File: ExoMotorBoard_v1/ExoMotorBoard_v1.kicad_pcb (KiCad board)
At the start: 2 copper layers, 3 parts, among them IC1 DSPIC33FJ128MC802-I_SP, U1 MIC5219-3.3YMM

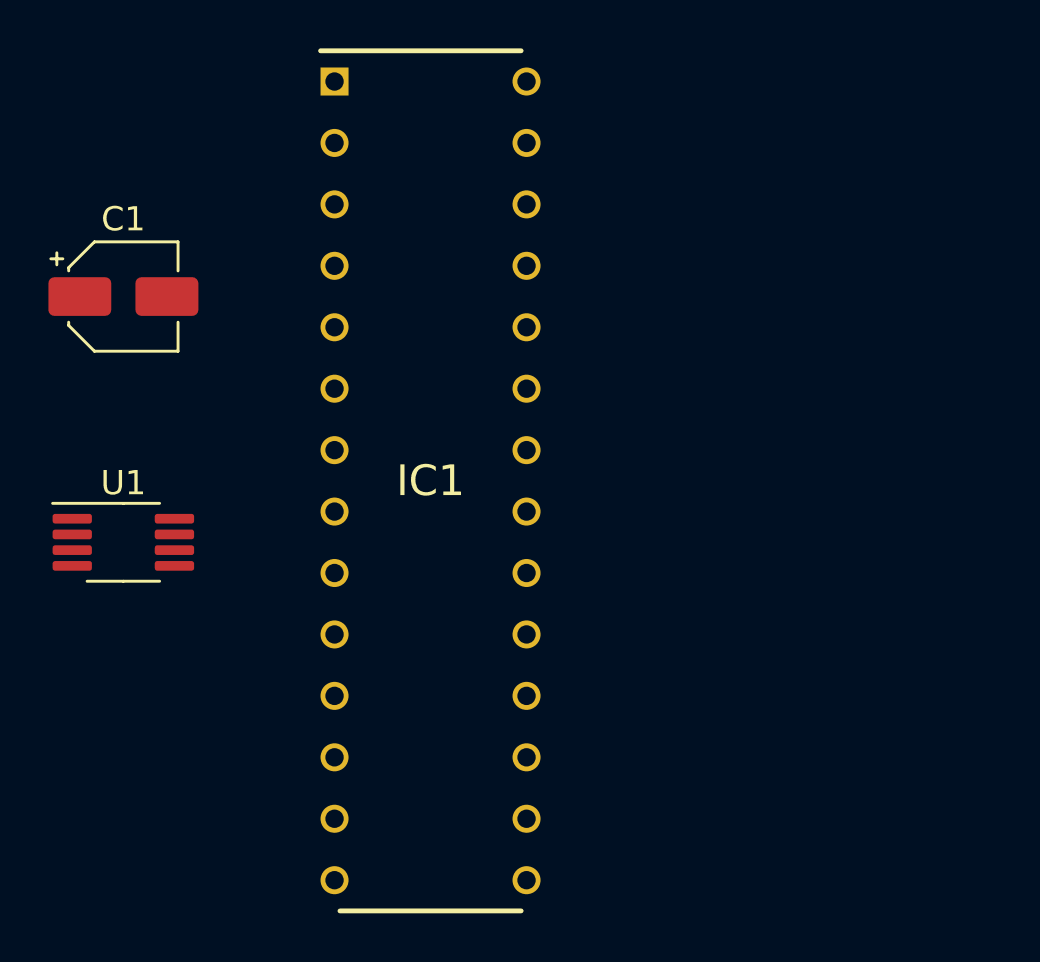
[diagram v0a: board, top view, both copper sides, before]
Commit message: 3.3v regulator circuit updated
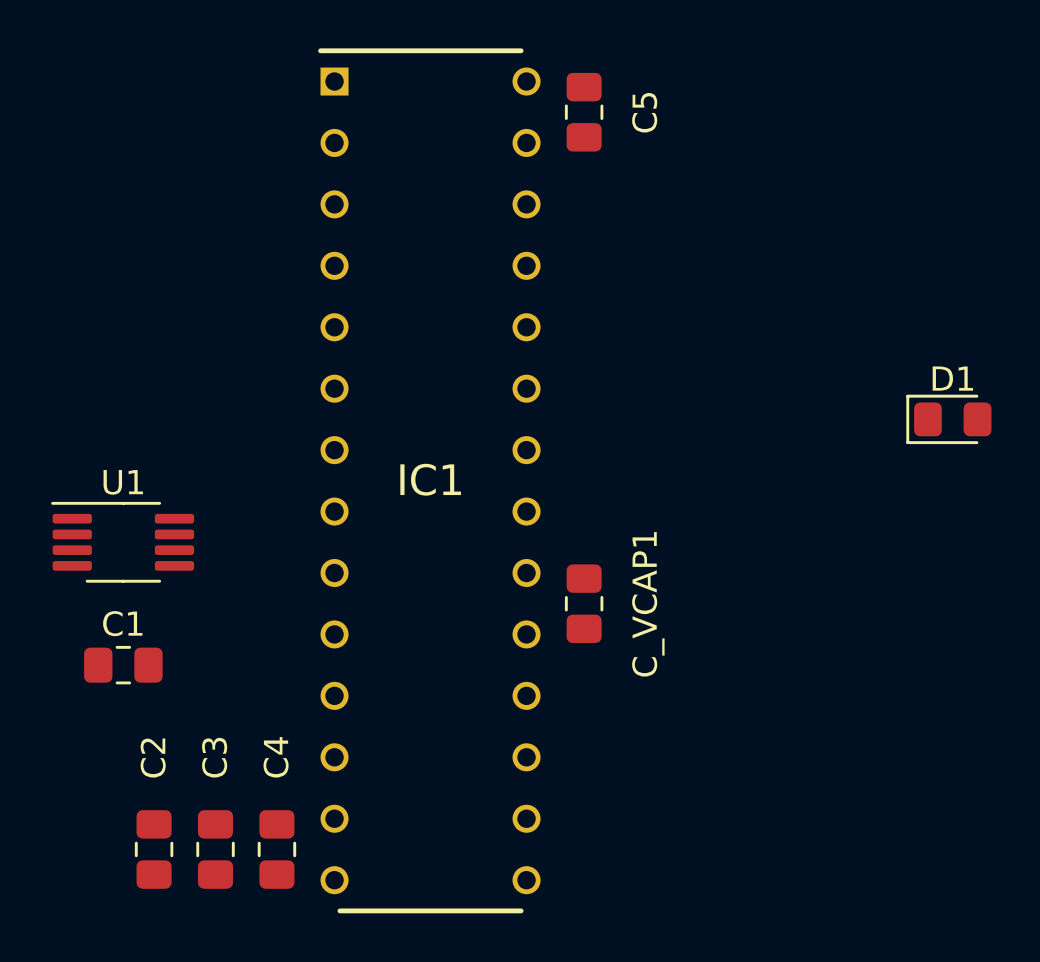
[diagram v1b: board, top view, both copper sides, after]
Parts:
- added C2: 0.1uF, Capacitor_SMD:C_0805_2012Metric_Pad1.18x1.45mm_HandSolder, F.Cu at (105.4, 74.9)
- added C3: 0.1uF, Capacitor_SMD:C_0805_2012Metric_Pad1.18x1.45mm_HandSolder, F.Cu at (108.0, 74.9)
- added C4: 0.1uF, Capacitor_SMD:C_0805_2012Metric_Pad1.18x1.45mm_HandSolder, F.Cu at (110.5, 74.9)
- added C5: 0.1uF, Capacitor_SMD:C_0805_2012Metric_Pad1.18x1.45mm_HandSolder, F.Cu at (123.2, 44.5)
- added C_VCAP1: 10uF, Capacitor_SMD:C_0805_2012Metric_Pad1.18x1.45mm_HandSolder, F.Cu at (123.2, 64.8)
- added D1: SML-H12P8TT86C, LED_SMD:LED_0805_2012Metric_Pad1.15x1.40mm_HandSolder, F.Cu at (138.4, 57.1)
- C1: value C -> 1uF; footprint Capacitor_SMD:CP_Elec_4x5.3 -> Capacitor_SMD:C_0805_2012Metric_Pad1.18x1.45mm_HandSolder
- moved C1 15.2 mm to (104.1, 67.3)
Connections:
- C1 pad 1: Net-(C1-Pad1) -> +3V3
- IC1 pad 13: Net-(IC1-Pad13) -> +3V3
- IC1 pad 19: Net-(IC1-Pad19) -> GND
- IC1 pad 27: Net-(IC1-Pad27) -> GND
- IC1 pad 8: Net-(IC1-Pad8) -> GND
- U1 pad 1: Net-(C1-Pad1) -> VIN
- U1 pad 2: Net-(U1-Pad2) -> VIN
- U1 pad 3: Net-(U1-Pad3) -> +3V3

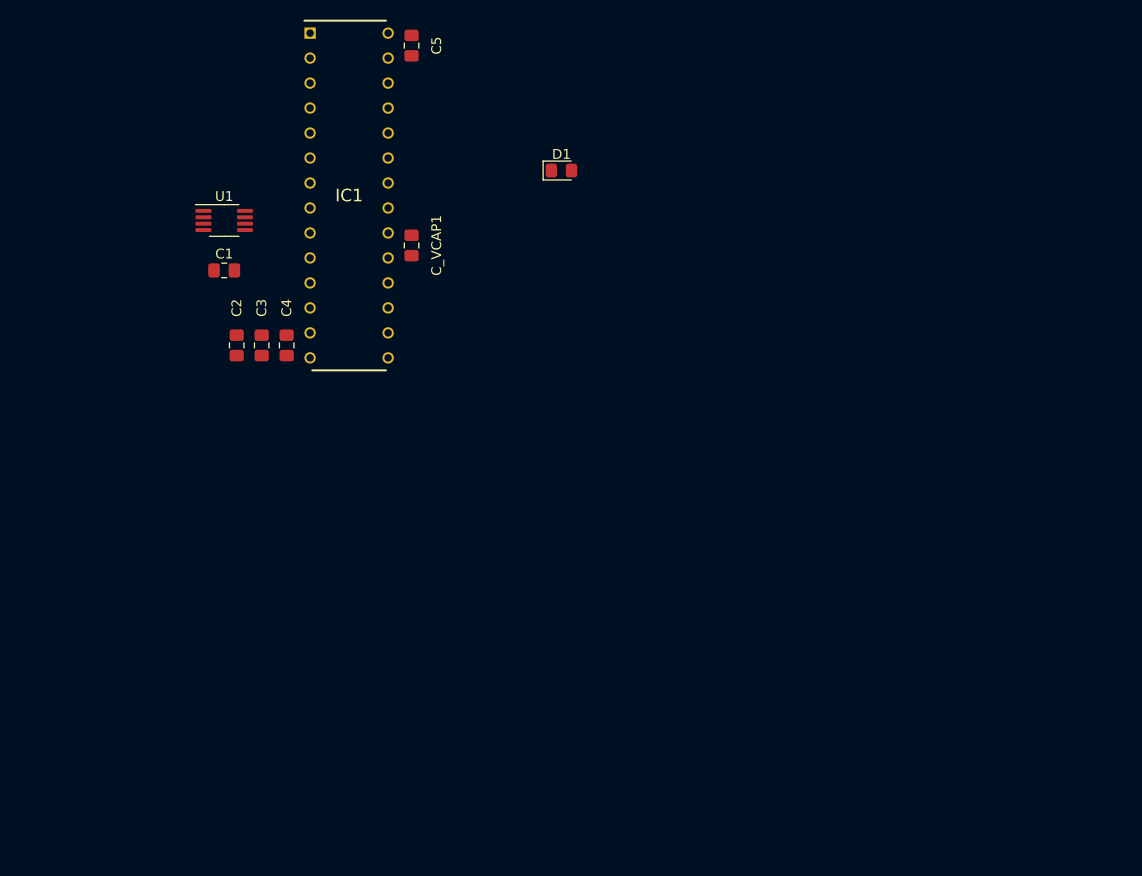
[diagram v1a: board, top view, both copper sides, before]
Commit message: Kicad project organized by modular sheets
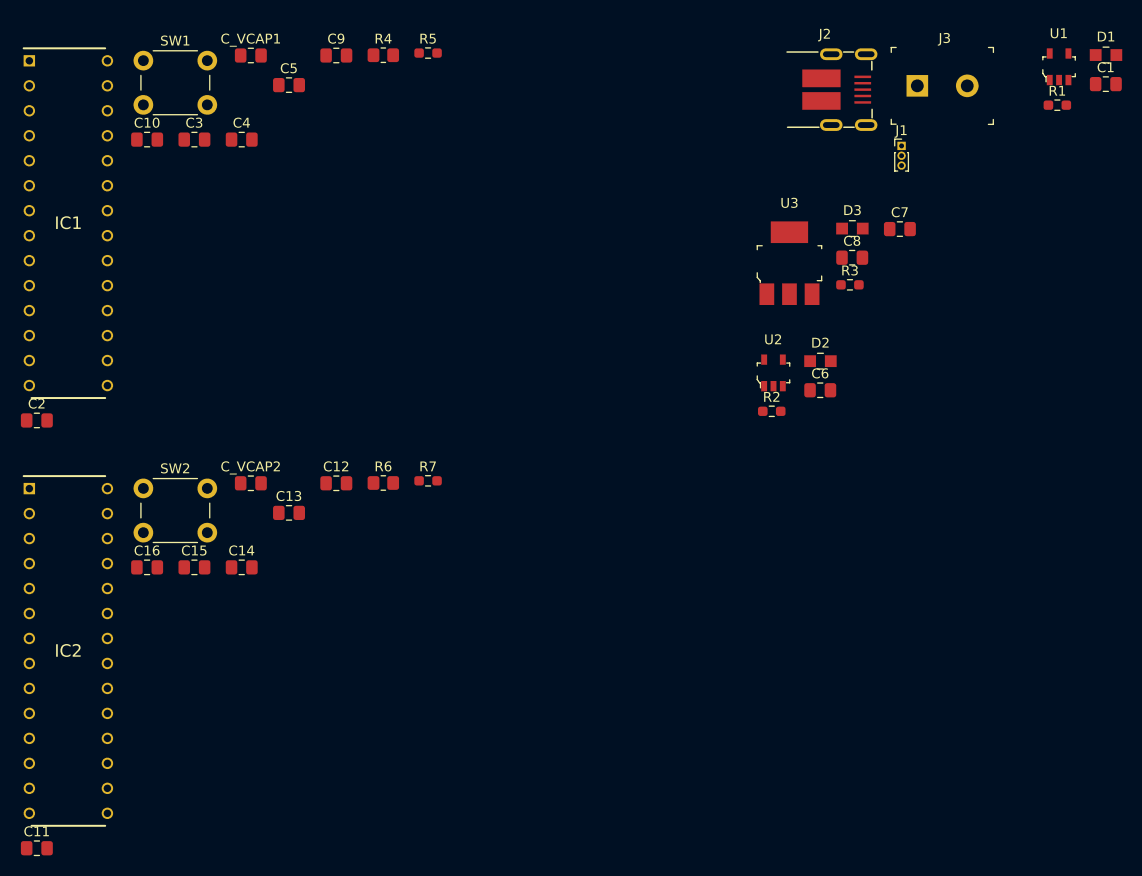
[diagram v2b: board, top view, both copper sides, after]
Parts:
- added C10: 0.1uF, Capacitor_SMD:C_0805_2012Metric_Pad1.18x1.45mm_HandSolder, F.Cu at (96.3, 54.0)
- added C11: 0.1uF, Capacitor_SMD:C_0805_2012Metric_Pad1.18x1.45mm_HandSolder, F.Cu at (85.1, 126.1)
- added C12: 0.1uF, Capacitor_SMD:C_0805_2012Metric_Pad1.18x1.45mm_HandSolder, F.Cu at (115.5, 89.0)
- added C13: 0.1uF, Capacitor_SMD:C_0805_2012Metric_Pad1.18x1.45mm_HandSolder, F.Cu at (110.7, 92.0)
- added C14: 0.1uF, Capacitor_SMD:C_0805_2012Metric_Pad1.18x1.45mm_HandSolder, F.Cu at (105.9, 97.5)
- added C15: 0.1uF, Capacitor_SMD:C_0805_2012Metric_Pad1.18x1.45mm_HandSolder, F.Cu at (101.1, 97.5)
- added C16: 0.1uF, Capacitor_SMD:C_0805_2012Metric_Pad1.18x1.45mm_HandSolder, F.Cu at (96.3, 97.5)
- added C6: 1uF, Capacitor_SMD:C_0805_2012Metric_Pad1.18x1.45mm_HandSolder, F.Cu at (164.8, 79.5)
- added C7: 10uF, Capacitor_SMD:C_0805_2012Metric_Pad1.18x1.45mm_HandSolder, F.Cu at (172.9, 63.1)
- added C8: 10uF, Capacitor_SMD:C_0805_2012Metric_Pad1.18x1.45mm_HandSolder, F.Cu at (168.0, 66.0)
- added C9: 0.1uF, Capacitor_SMD:C_0805_2012Metric_Pad1.18x1.45mm_HandSolder, F.Cu at (115.5, 45.5)
- added C_VCAP2: 10uF, Capacitor_SMD:C_0805_2012Metric_Pad1.18x1.45mm_HandSolder, F.Cu at (106.9, 89.0)
- added D2: LG_R971-KN-1, digikey-footprints:0805, F.Cu at (164.8, 76.5)
- added D3: LG_R971-KN-1, digikey-footprints:0805, F.Cu at (168.0, 63.1)
- added IC2: DSPIC33FJ128MC802-I_SP, DSPIC33FJ128MC802-I_SP:DIP794W56P254L3486H508Q28N, F.Cu at (88.3, 106.0)
- added J1: Conn_01x03_Male, Connector_PinHeader_1.00mm:PinHeader_1x03_P1.00mm_Vertical, F.Cu at (173.0, 54.6)
- added J2: UJ2-MIBH-4-SMT-TR, digikey-footprints:USB_Micro_B_Male_UJ2-MIBH-4-SMT-TR, F.Cu at (161.2, 48.9)
- added J3: OSTTC022162, digikey-footprints:Term_Block_1x2_P5.08MM, F.Cu at (174.6, 48.5)
- added R1: 3.3k, Resistor_SMD:R_0603_1608Metric_Pad0.98x0.95mm_HandSolder, F.Cu at (188.9, 50.5)
- added R2: 3.3k, Resistor_SMD:R_0603_1608Metric_Pad0.98x0.95mm_HandSolder, F.Cu at (159.8, 81.6)
- added R3: 3.3k, Resistor_SMD:R_0603_1608Metric_Pad0.98x0.95mm_HandSolder, F.Cu at (167.8, 68.8)
- added R4: 10k, Resistor_SMD:R_0805_2012Metric_Pad1.20x1.40mm_HandSolder, F.Cu at (120.3, 45.4)
- added R5: 400, Resistor_SMD:R_0603_1608Metric_Pad0.98x0.95mm_HandSolder, F.Cu at (124.9, 45.2)
- added R6: 10k, Resistor_SMD:R_0805_2012Metric_Pad1.20x1.40mm_HandSolder, F.Cu at (120.3, 88.9)
- added R7: 400, Resistor_SMD:R_0603_1608Metric_Pad0.98x0.95mm_HandSolder, F.Cu at (124.9, 88.7)
- added SW1: SW_Push_Dual, Button_Switch_THT:SW_PUSH_6mm_H5mm, F.Cu at (95.9, 46.0)
- added SW2: SW_Push_Dual, Button_Switch_THT:SW_PUSH_6mm_H5mm, F.Cu at (95.9, 89.5)
- added U2: MIC5219-3_3YM5-TR, digikey-footprints:SOT-753, F.Cu at (160.0, 77.7)
- added U3: NCP1117ST50T3G, digikey-footprints:SOT-223, F.Cu at (161.6, 66.6)
- D1: value SML-H12P8TT86C -> LG_R971-KN-1; footprint LED_SMD:LED_0805_2012Metric_Pad1.15x1.40mm_HandSolder -> digikey-footprints:0805
- U1: value MIC5219-3.3YMM -> MIC5219-3_3YM5-TR; footprint Package_SO:MSOP-8_3x3mm_P0.65mm -> digikey-footprints:SOT-753
- moved C1 91.6 mm to (193.8, 48.4)
- moved U1 86.3 mm to (189.0, 46.6)
- moved D1 56.6 mm to (193.8, 45.4)
- moved IC1 28.7 mm to (88.3, 62.5)
- moved C_VCAP1 25.3 mm to (106.9, 45.5), turned to 0 degrees
- moved C3 22.0 mm to (101.1, 54.0), turned to 0 degrees
- moved C2 21.7 mm to (85.1, 82.6), turned to 0 degrees
- moved C4 21.4 mm to (105.9, 54.0), turned to 0 degrees
- moved C5 13.1 mm to (110.7, 48.5), turned to 0 degrees
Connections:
- net Net-(C_VCAP1-Pad2) renamed /MCU_Circuit1/VCAP
- net Net-(IC1-Pad16) renamed /MCU_Circuit1/QEI1_I
- net Net-(IC1-Pad17) renamed /MCU_Circuit1/QEI1_B
- net Net-(IC1-Pad18) renamed /MCU_Circuit1/QEI1_A
- C1 pad 1: +3V3 -> /VDD_1
- C2 pad 1: GND -> /VDD_1
- C2 pad 2: +3V3 -> /MCU_Circuit1/VSS
- C3 pad 1: GND -> /VDD_1
- C3 pad 2: +3V3 -> /MCU_Circuit1/VSS
- C4 pad 1: GND -> /VDD_1
- C4 pad 2: +3V3 -> /MCU_Circuit1/VSS
- C5 pad 1: GND -> /VDD_1
- C5 pad 2: Net-(C5-Pad2) -> /MCU_Circuit1/VSS
- C_VCAP1 pad 1: GND -> /MCU_Circuit1/VSS
- D1 pad 1: GND -> Net-(D1-Pad1)
- D1 pad 2: Net-(D1-Pad2) -> GND
- IC1 pad 1: Net-(IC1-Pad1) -> /MCU_Circuit1/MSCLR
- IC1 pad 13: +3V3 -> /VDD_1
- IC1 pad 19: GND -> /MCU_Circuit1/VSS
- IC1 pad 27: GND -> /MCU_Circuit1/AVSS
- IC1 pad 28: Net-(C5-Pad2) -> /MCU_Circuit1/AVDD
- IC1 pad 8: GND -> /MCU_Circuit1/VSS
- U1 pad 1: VIN -> /PowerCircuit/Vin
- U1 pad 2: VIN -> GND
- U1 pad 3: +3V3 -> /PowerCircuit/Vin
- U1 pad 5: GND -> /VDD_1

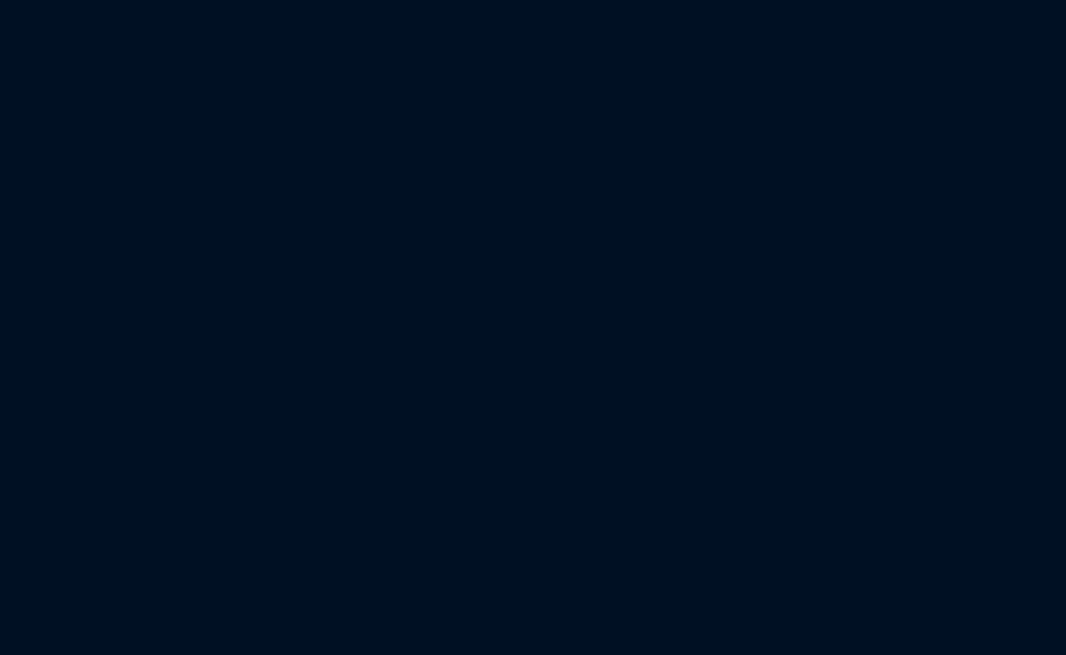
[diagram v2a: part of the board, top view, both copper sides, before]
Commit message: MCU connection updated
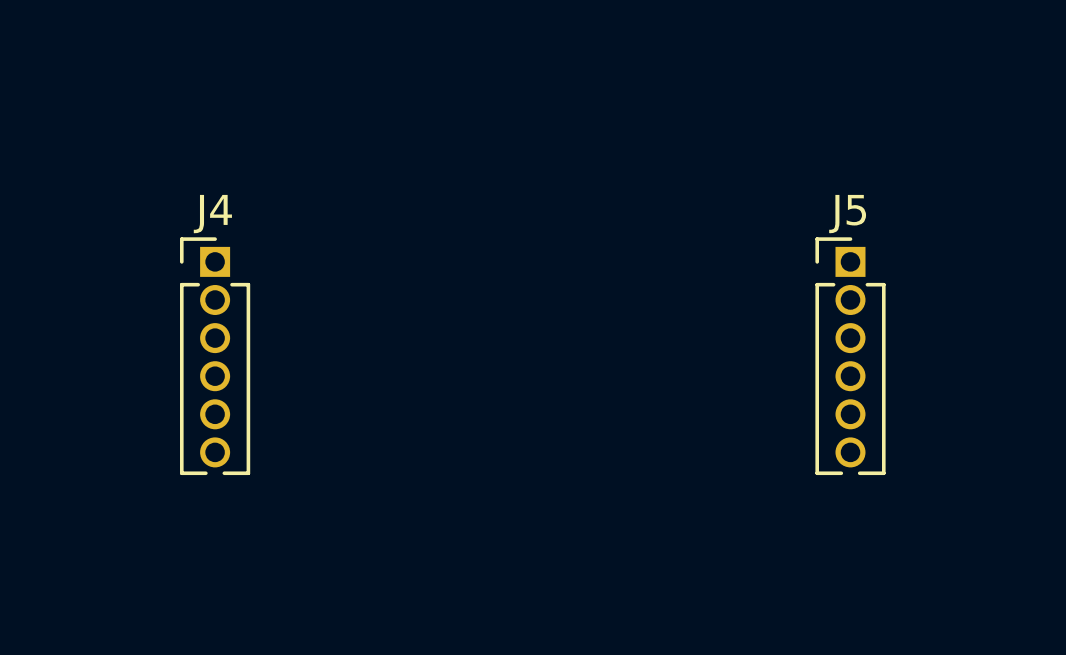
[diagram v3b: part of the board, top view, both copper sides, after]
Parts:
- added J4: Conn_01x06_Male, Connector_PinHeader_1.27mm:PinHeader_1x06_P1.27mm_Vertical, F.Cu at (156.2, 104.8)
- added J5: Conn_01x06_Male, Connector_PinHeader_1.27mm:PinHeader_1x06_P1.27mm_Vertical, F.Cu at (177.4, 104.8)
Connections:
- net Net-(IC1-Pad14) renamed /MCU_Circuit1/QEI2_I
- net Net-(IC1-Pad2) renamed /MCU_Circuit1/AN0_INPUT
- net Net-(IC1-Pad21) renamed /MCU_Circuit1/QEI2_B
- net Net-(IC1-Pad22) renamed /MCU_Circuit1/QEI2_A
- net Net-(IC1-Pad25) renamed /MCU_Circuit1/PWM_1H
- net Net-(IC1-Pad3) renamed /MCU_Circuit1/AN1_INPUT
- net Net-(IC2-Pad14) renamed /MCU_Circuit2/QEI2_I
- net Net-(IC2-Pad2) renamed /MCU_Circuit2/AN0_INPUT
- net Net-(IC2-Pad21) renamed /MCU_Circuit2/QEI2_B
- net Net-(IC2-Pad22) renamed /MCU_Circuit2/QEI2_A
- net Net-(IC2-Pad25) renamed /MCU_Circuit2/PWM_1H
- net Net-(IC2-Pad3) renamed /MCU_Circuit2/AN1_INPUT
- C10 pad 1: /MCU_Circuit1/AVDD -> /VDD_1
- C11 pad 2: /MCU_Circuit2/VSS -> GND
- C12 pad 2: /MCU_Circuit2/VSS -> GND
- C13 pad 2: /MCU_Circuit2/VSS -> GND
- C14 pad 2: /MCU_Circuit2/VSS -> GND
- C15 pad 2: /MCU_Circuit2/VSS -> GND
- C16 pad 1: /MCU_Circuit2/AVDD -> /VDD_2
- C2 pad 2: /MCU_Circuit1/VSS -> GND
- C3 pad 2: /MCU_Circuit1/VSS -> GND
- C4 pad 2: /MCU_Circuit1/VSS -> GND
- C5 pad 2: /MCU_Circuit1/VSS -> GND
- C9 pad 2: /MCU_Circuit1/VSS -> GND
- C_VCAP1 pad 1: /MCU_Circuit1/VSS -> GND
- C_VCAP2 pad 1: /MCU_Circuit2/VSS -> GND
- IC1 pad 19: /MCU_Circuit1/VSS -> GND
- IC1 pad 28: /MCU_Circuit1/AVDD -> /VDD_1
- IC1 pad 4: Net-(IC1-Pad4) -> /MCU_Circuit1/AN2_INPUT
- IC1 pad 5: Net-(IC1-Pad5) -> /MCU_Circuit1/AN3_INPUT
- IC1 pad 8: /MCU_Circuit1/VSS -> GND
- IC2 pad 19: /MCU_Circuit2/VSS -> GND
- IC2 pad 28: /MCU_Circuit2/AVDD -> /VDD_2
- IC2 pad 4: Net-(IC2-Pad4) -> /MCU_Circuit2/AN2_INPUT
- IC2 pad 5: Net-(IC2-Pad5) -> /MCU_Circuit2/AN3_INPUT
- IC2 pad 8: /MCU_Circuit2/VSS -> GND
- SW1 pad 2: /MCU_Circuit1/VSS -> GND
- SW2 pad 2: /MCU_Circuit2/VSS -> GND
